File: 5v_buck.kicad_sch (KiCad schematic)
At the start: 11 parts, among them J2 SERVO_BUCK_IN, J3 SERVO_BUCK_OUT, J4 Servo1, J5 Servo2, J6 Servo3, J7 Servo4, J8 Servo5

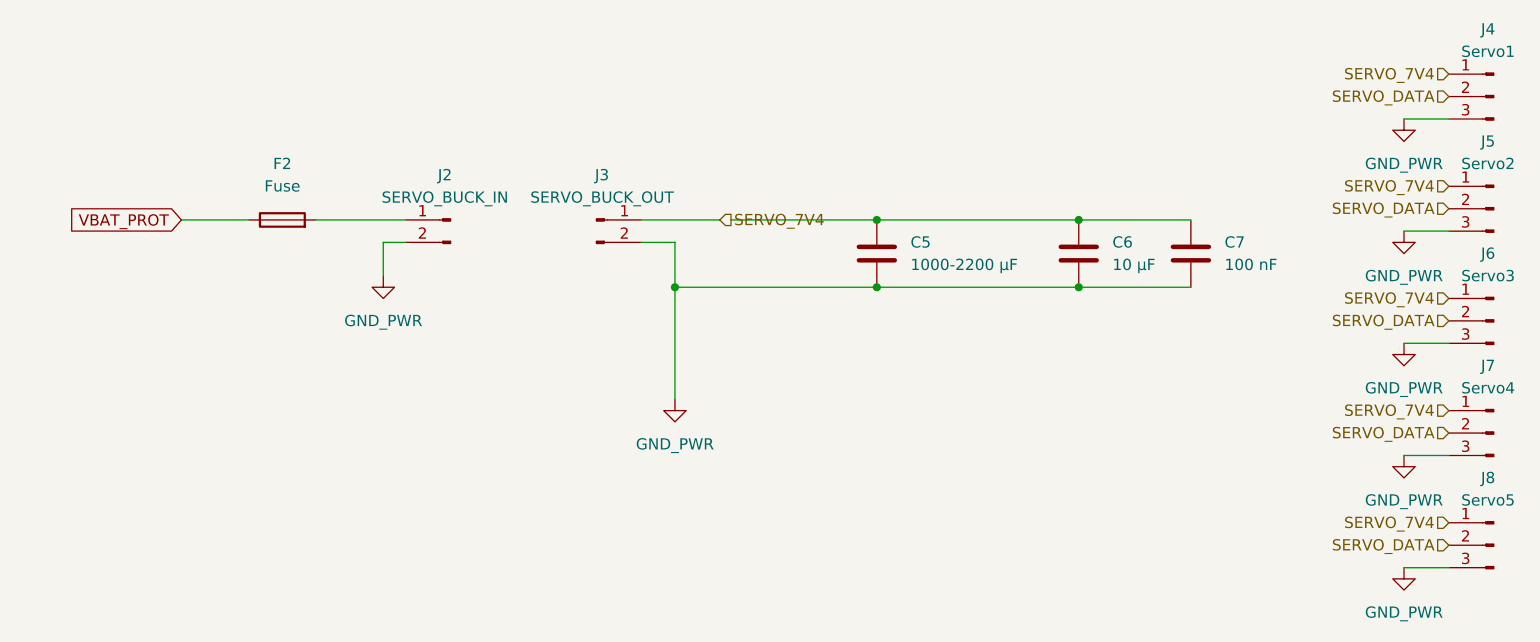
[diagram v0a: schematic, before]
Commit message: added 5v buck converter and place JST PH connectors
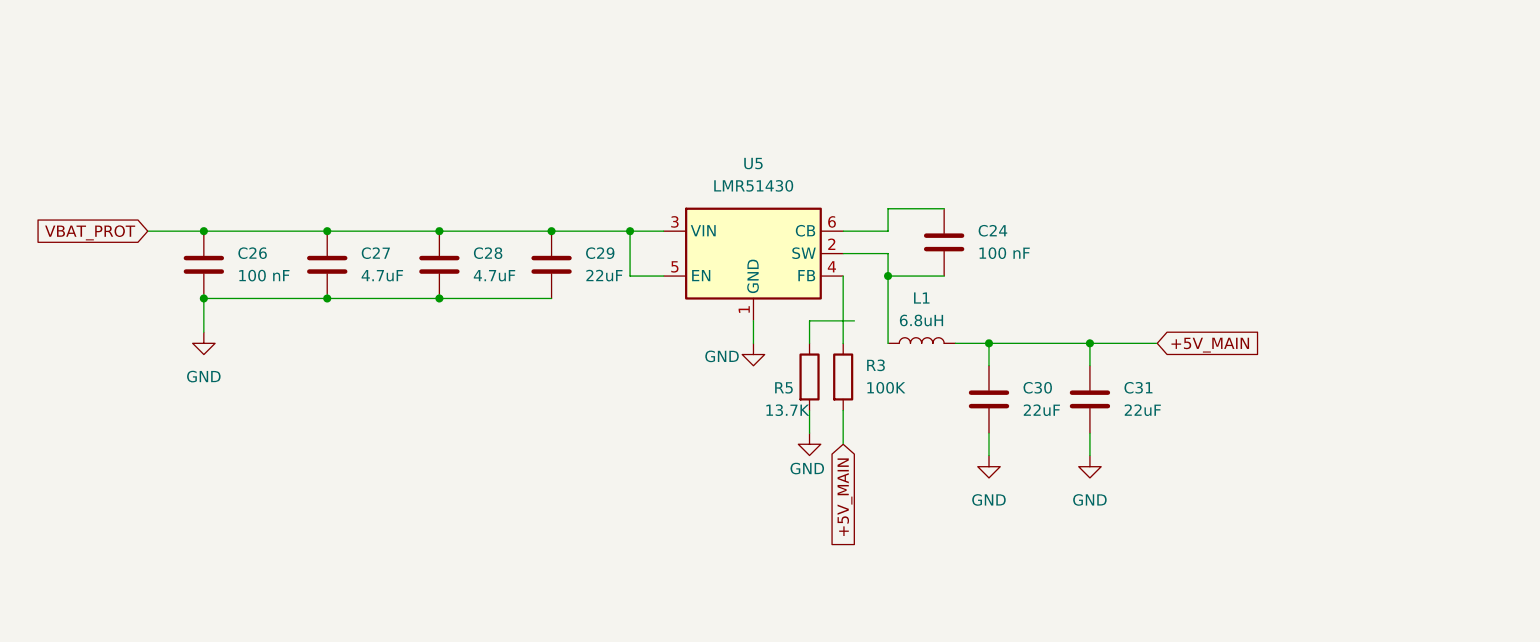
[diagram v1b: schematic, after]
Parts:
- removed C5: 1000-2200 µF, Capacitor_SMD:C_0805_2012Metric_Pad1.18x1.45mm_HandSolder, symbol Device:C
- removed C6: 10 µF, Capacitor_SMD:C_0805_2012Metric_Pad1.18x1.45mm_HandSolder, symbol Device:C
- removed C7: 100 nF, Capacitor_SMD:C_0805_2012Metric_Pad1.18x1.45mm_HandSolder, symbol Device:C
- removed F2: Fuse, Fuse:Fuse_0805_2012Metric_Pad1.15x1.40mm_HandSolder, symbol Device:Fuse
- removed J2: SERVO_BUCK_IN, symbol Connector:Conn_01x02_Pin
- removed J3: SERVO_BUCK_OUT, symbol Connector:Conn_01x02_Pin
- removed J4: Servo1, symbol Connector:Conn_01x03_Pin
- removed J5: Servo2, symbol Connector:Conn_01x03_Pin
- removed J6: Servo3, symbol Connector:Conn_01x03_Pin
- removed J7: Servo4, symbol Connector:Conn_01x03_Pin
- removed J8: Servo5, symbol Connector:Conn_01x03_Pin
- added C24, C26: 100 nF, symbol Device:C
- added C27, C28: 4.7uF, symbol Device:C
- added C29, C30, C31: 22uF, symbol Device:C
- added L1: 6.8uH, symbol Device:L
- added R3: 100K, symbol Device:R
- added R5: 13.7K, symbol Device:R
- added U5: LMR51430, Package_TO_SOT_SMD:SOT-23-6, symbol Regulator_Switching:LMR51430
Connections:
- net VBAT_PROT: now also C26.1, C27.1, C28.1, C29.1, U5.3 (VIN), U5.5 (EN)
- new net: C24.2, L1.1, U5.2 (SW)
- new net: R3.1, U5.4 (FB)
- new net: C24.1, U5.6 (CB)
- new net +5V_MAIN: C30.1, C31.1, L1.2, R3.2
- new net GND: C26.2, C27.2, C28.2, C29.2, C30.2, C31.2, R5.2, U5.1 (GND)

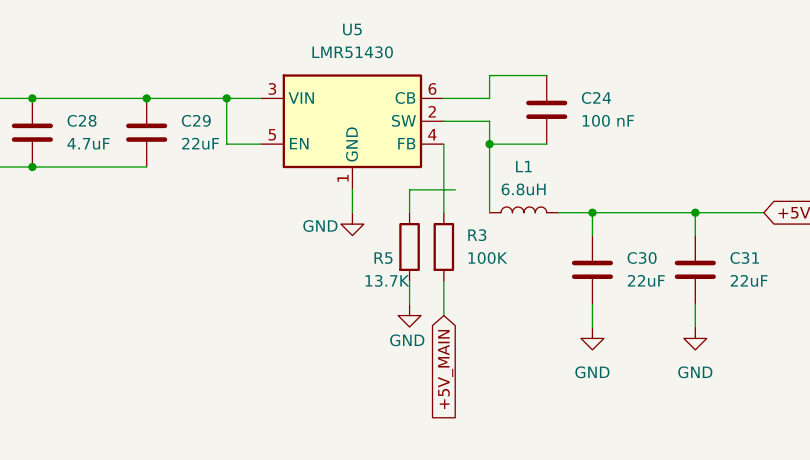
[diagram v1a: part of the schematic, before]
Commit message: fix 5v_buck scheme and delete bad name scheme
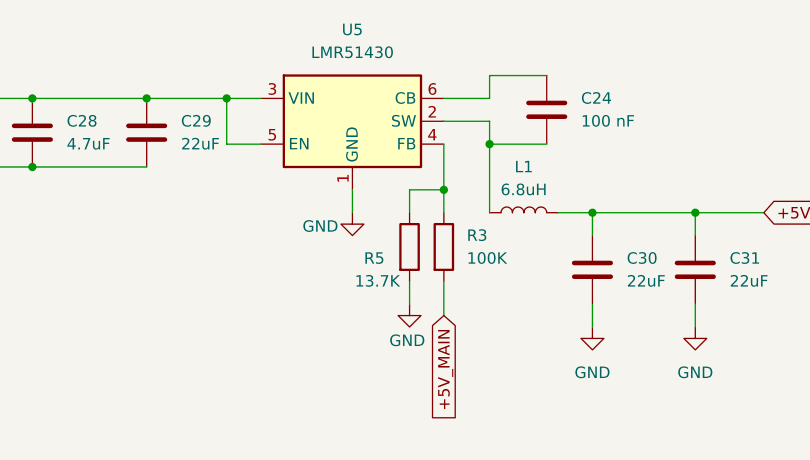
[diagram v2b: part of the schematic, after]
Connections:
- net at R3.1, U5.4 (FB): now also R5.1
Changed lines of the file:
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@@
+	)
+	(junction
+		(at 146.05 101.6)
+		(diameter 0)
+		(color 0 0 0 0)
 	)
 	(junction
@@
 	(wire
 		(pts
+			(xy 146.05 101.6) (xy 146.05 104.14)
+		)
+		(stroke
+			(width 0)
+			(type default)
+		)
+	)
+	(wire
+		(pts
+			(xy 142.24 111.76) (xy 142.24 114.3)
+		)
+		(stroke
+			(width 0)
+			(type default)
+		)
+	)
+	(wire
+		(pts
 			(xy 158.75 104.14) (xy 162.56 104.14)
 		)
@@
 	(wire
 		(pts
-			(xy 146.05 96.52) (xy 146.05 104.14)
+			(xy 146.05 96.52) (xy 146.05 101.6)
 		)
 		(stroke
@@
 	(wire
 		(pts
+			(xy 142.24 101.6) (xy 146.05 101.6)
+		)
+		(stroke
+			(width 0)
+			(type default)
+		)
+	)
+	(wire
+		(pts
 			(xy 87.63 99.06) (xy 100.33 99.06)
 		)
@@
 		(pts
 			(xy 113.03 91.44) (xy 121.92 91.44)
-		)
-		(stroke
-			(width 0)
-			(type default)
-		)
-	)
-	(wire
-		(pts
-			(xy 142.24 111.76) (xy 142.24 114.3)
-		)
-		(stroke
-			(width 0)
-			(type default)
-		)
-	)
-	(wire
-		(pts
-			(xy 147.32 101.6) (xy 142.24 101.6)
 		)
 		(stroke
@@
 		(dnp no)
 		(property "Reference" "R5"
-			(at 138.176 109.22 0)
+			(at 137.16 109.22 0)
 			(show_name no)
 			(do_not_autoplace no)
@@
 		)
 		(property "Value" "13.7K"
-			(at 137.16 111.76 0)
-			(show_name no)
-			(do_not_autoplace no)
+			(at 136.144 111.76 0)
+			(show_name no)
+			(do_not_autoplace no)
